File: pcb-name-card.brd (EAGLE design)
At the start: 87.5 x 54 mm, 7 parts

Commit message: aa banner
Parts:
- moved SW2 27.6 mm to (35.6, 5.70)
- moved SW1 27.4 mm to (35.7, 48.9)
- moved R1 14.2 mm to (64.3, 43.2), turned to 220 degrees
- moved R2 12.9 mm to (63.4, 10.7), turned to 145 degrees
- moved LED2 2.97 mm to (81.8, 23.1)
- moved U$1 1.21 mm to (12.1, 28.5)
- moved LED1 0.80 mm to (82.1, 31.8)
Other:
- board text added: "E:/Dropbox/git-projects/pcb-name-card/algoaccess banner.bmp"

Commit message: more changes
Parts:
- moved R1 8.28 mm to (58.6, 49.2), turned to 25 degrees
- moved R2 7.61 mm to (59.6, 4.11), turned to 335 degrees
- moved LED1 3.71 mm to (84.7, 34.4), turned to 0 degrees
- moved LED2 3.37 mm to (85.1, 22.4), turned to 0 degrees
- moved U$1 1.69 mm to (10.7, 27.6)
- moved SW1 1.27 mm to (35.7, 47.6)
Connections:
- net N$3: now also SW1.COM1; no longer SW1.COM2, U$1.+$2
- net N$4: now also SW1.CH2A; no longer SW1.CH1A
- net N$7: now also U$1.+$2; no longer SW1.COM1
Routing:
- net N$7: track 0.00 -> 28.2 mm
- net N$2: track 0.00 -> 27.0 mm
- net N$3: track 0.00 -> 26.9 mm
- net N$1: track 0.00 -> 25.3 mm
- net N$5: track 0.00 -> 18.0 mm
- net N$4: track 0.00 -> 17.0 mm
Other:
- board size 87.5 x 54 mm -> 87.5 x 53.3 mm
- board text added: "E:/Dropbox/git-projects/pcb-name-card/algoaccess banner mirror.bmp"

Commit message: some changes
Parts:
- moved R2 1.16 mm to (58.5, 4.39), turned to 330 degrees
- moved U$1 1.04 mm to (10.6, 26.5)
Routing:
- net N$6: track 0.00 -> 169.7 mm
- net N$7: track 28.2 -> 27.2 mm
- net N$5: track 18.0 -> 17.0 mm
- net N$2: track 27.0 -> 27.8 mm
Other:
- board text added: "Caution: Look away from LEDs before toggling the switches"
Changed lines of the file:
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@@
 <layer number="26" name="bNames" color="7" fill="1" visible="yes" active="yes"/>
 <layer number="27" name="tValues" color="7" fill="1" visible="no" active="yes"/>
-<layer number="28" name="bValues" color="7" fill="1" visible="no" active="yes"/>
+<layer number="28" name="bValues" color="7" fill="1" visible="yes" active="yes"/>
 <layer number="29" name="tStop" color="7" fill="3" visible="no" active="yes"/>
 <layer number="30" name="bStop" color="7" fill="6" visible="no" active="yes"/>
@@
 <layer number="43" name="vRestrict" color="2" fill="10" visible="no" active="yes"/>
 <layer number="44" name="Drills" color="7" fill="1" visible="no" active="yes"/>
-<layer number="45" name="Holes" color="7" fill="1" visible="yes" active="yes"/>
-<layer number="46" name="Milling" color="3" fill="1" visible="yes" active="yes"/>
+<layer number="45" name="Holes" color="7" fill="1" visible="no" active="yes"/>
+<layer number="46" name="Milling" color="3" fill="1" visible="no" active="yes"/>
 <layer number="47" name="Measures" color="7" fill="1" visible="no" active="yes"/>
 <layer number="48" name="Document" color="7" fill="1" visible="no" active="yes"/>
@@
 <layer number="120" name="KAP_MAAT1" color="7" fill="1" visible="no" active="no"/>
 <layer number="121" name="_tsilk" color="7" fill="1" visible="no" active="yes"/>
-<layer number="122" name="_bsilk" color="7" fill="1" visible="no" active="yes"/>
+<layer number="122" name="_bsilk" color="7" fill="1" visible="yes" active="yes"/>
 <layer number="123" name="tTestmark" color="7" fill="1" visible="no" active="yes"/>
 <layer number="124" name="bTestmark" color="7" fill="1" visible="no" active="yes"/>
@@
 <rectangle x1="53.29428125" y1="46.0400375" x2="53.721" y2="46.0705125" layer="22"/>
 <text x="0" y="-0.1524" size="0.060959375" layer="22" font="vector" rot="MR0">E:/Dropbox/git-projects/pcb-name-card/algoaccess banner mirror.bmp</text>
+<text x="30.9372" y="4.693921875" size="1.27" layer="22" font="vector" rot="MR0">Caution: Look away from LEDs
+before toggling the switches</text>
 </plain>
 <attributes>
@@
 <element name="LED1" library="led" package="PLCC2" value="UV" x="84.65185" y="34.44875" smashed="yes" rot="MR0">
 <attribute name="COLOR" value="yellow" x="84.65185" y="34.44875" size="1.778" layer="28" rot="MR0" display="off"/>
-<attribute name="VALUE" x="80.84185" y="32.54375" size="1.27" layer="28" rot="MR90"/>
+<attribute name="VALUE" x="80.84185" y="33.214309375" size="1.27" layer="28" rot="MR90"/>
 </element>
 <element name="LED2" library="led" package="CHIP-LED0805" value="Light" x="85.09635" y="22.39645" smashed="yes" rot="MR0">
-<attribute name="VALUE" x="81.9531" y="19.8247" size="1.27" layer="28" rot="MR90"/>
+<attribute name="VALUE" x="82.0140625" y="19.5808625" size="1.27" layer="28" rot="MR90"/>
 </element>
-<element name="U$1" library="cr2032" package="CR2032-SMD" value="" x="10.6807" y="27.570428125" smashed="yes" rot="MR270">
-<attribute name="VALUE" x="23.0307" y="31.888428125" size="1.6764" layer="28" font="vector" rot="MR270"/>
+<element name="U$1" library="cr2032" package="CR2032-SMD" value="" x="10.558778125" y="26.534109375" smashed="yes" rot="MR270">
+<attribute name="VALUE" x="22.908778125" y="30.852109375" size="1.6764" layer="28" font="vector" rot="MR270"/>
 </element>
 <element name="SW1" library="Seeed-OPL-Switch" package="SW6-2.54-SMD-7.0X3.5X1.5MM" value="" x="35.6743" y="47.63135" smashed="yes" rot="MR90">
@@
 </element>
 <element name="R1" library="resistor" package="0207/7" value="" x="58.6232" y="49.1998" smashed="yes" rot="MR25">
-<attribute name="NAME" x="59.17851875" y="48.488415625" size="1.27" layer="26" ratio="10" rot="MR25"/>
+<attribute name="NAME" x="59.239478125" y="48.244575" size="1.27" layer="26" ratio="10" rot="MR25"/>
 <attribute name="VALUE" x="60.458859375" y="47.72725" size="1.27" layer="28" ratio="10" rot="MR25"/>
 </element>
-<element name="R2" library="resistor" package="0207/7" value="" x="59.5884" y="4.1148" smashed="yes" rot="MR335">
-<attribute name="NAME" x="60.47875625" y="3.87030625" size="1.27" layer="26" ratio="10" rot="MR335"/>
-<attribute name="VALUE" x="61.89638125" y="4.5744625" size="1.27" layer="28" ratio="10" rot="MR335"/>
+<element name="R2" library="resistor" package="0207/7" value="" x="58.460640625" y="4.38911875" smashed="yes" rot="MR330">
+<attribute name="NAME" x="59.368915625" y="4.223153125" size="1.27" layer="26" ratio="10" rot="MR330"/>
+<attribute name="VALUE" x="60.719775" y="5.048184375" size="1.27" layer="28" ratio="10" rot="MR330"/>
 </element>
 </elements>
@@
 <contactref element="R2" pad="1"/>
 <contactref element="LED2" pad="A"/>
-<wire x1="63.041434375" y1="5.724975" x2="85.09635" y2="21.34645" width="0.4064" layer="16"/>
+<wire x1="61.7602" y1="6.29411875" x2="85.09635" y2="21.34645" width="0.4064" layer="16"/>
 </signal>
 <signal name="N$6">
@@
 <contactref element="LED1" pad="C"/>
 <contactref element="LED2" pad="C"/>
-<wire x1="85.09635" y1="23.44645" x2="84.65185" y2="32.74875" width="0" layer="19" extent="16-16"/>
-<wire x1="10.6807" y1="27.570428125" x2="84.65185" y2="32.74875" width="0" layer="19" extent="16-16"/>
+<wire x1="84.65185" y1="32.74875" x2="51.816" y2="49.408078125" width="0.4064" layer="16"/>
+<wire x1="51.816" y1="49.408078125" x2="10.558778125" y2="26.534109375" width="0.4064" layer="16"/>
+<wire x1="85.09635" y1="23.44645" x2="51.63311875" y2="3.84048125" width="0.4064" layer="16"/>
+<wire x1="51.63311875" y1="3.84048125" x2="10.558778125" y2="26.534109375" width="0.4064" layer="16"/>
 </signal>
 <signal name="N$3">
 <contactref element="U$1" pad="+$1"/>
 <contactref element="SW1" pad="COM1"/>
-<wire x1="10.6807" y1="39.000428125" x2="28.9179" y2="38.96995" width="0.4064" layer="16"/>
-<wire x1="28.9179" y1="38.96995" x2="35.6743" y2="44.45635" width="0.4064" layer="16"/>
+<wire x1="10.558778125" y1="37.964109375" x2="26.86558125" y2="37.964109375" width="0.4064" layer="16"/>
+<wire x1="26.86558125" y1="37.964109375" x2="35.6743" y2="44.45635" width="0.4064" layer="16"/>
 </signal>
 <signal name="N$7">
 <contactref element="U$1" pad="+$2"/>
 <contactref element="SW2" pad="COM2"/>
-<wire x1="10.6807" y1="16.140428125" x2="28.956" y2="16.1544" width="0.4064" layer="16"/>
-<wire x1="28.956" y1="16.1544" x2="35.6362" y2="8.87095" width="0.4064" layer="16"/>
+<wire x1="10.558778125" y1="15.104109375" x2="27.3913625" y2="15.104109375" width="0.4064" layer="16"/>
+<wire x1="27.3913625" y1="15.104109375" x2="35.6362" y2="8.87095" width="0.4064" layer="16"/>
 </signal>
 <signal name="N$5">
 <contactref element="R2" pad="2"/>
 <contactref element="SW2" pad="CH1A"/>
-<wire x1="56.13536875" y1="2.504621875" x2="38.1762" y2="2.52095" width="0.4064" layer="16"/>
+<wire x1="55.161084375" y1="2.484115625" x2="38.1762" y2="2.52095" width="0.4064" layer="16"/>
 </signal>
 <signal name="N$4">

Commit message: some updates
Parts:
- moved R2 12.1 mm to (69.5, 9.28)
- moved R1 10.7 mm to (68.4, 44.7)
- moved SW2 4.90 mm to (35.9, 10.6)
- moved SW1 4.55 mm to (36.3, 43.1)
- moved LED2 2.77 mm to (83.9, 19.9), turned to 180 degrees
- moved LED1 1.77 mm to (83.6, 33.0), turned to 180 degrees
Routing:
- net N$6: track 169.7 -> 220.7 mm
- net N$2: track 27.8 -> 14.8 mm
- net N$5: track 17.0 -> 27.7 mm
- net N$4: track 17.0 -> 26.1 mm
- net N$1: track 25.3 -> 16.7 mm
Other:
- board text added: "CR2025"

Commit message: more changes
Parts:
- moved SW1 2.54 mm to (36.3, 40.6)
- moved SW2 2.54 mm to (35.9, 13.1)
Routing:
- net N$7: track 27.0 -> 30.4 mm
- net N$3: track 27.4 -> 30.1 mm
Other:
- board text added: "Rev 1"
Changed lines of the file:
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@@
 <grid distance="0.1" unitdist="inch" unit="inch" style="lines" multiple="1" display="yes" altdistance="0.025" altunitdist="inch" altunit="inch"/>
 <layers>
-<layer number="1" name="Top" color="4" fill="1" visible="yes" active="yes"/>
+<layer number="1" name="Top" color="4" fill="1" visible="no" active="yes"/>
 <layer number="2" name="Route2" color="1" fill="3" visible="no" active="no"/>
 <layer number="3" name="Route3" color="4" fill="3" visible="no" active="no"/>
@@
 <layer number="19" name="Unrouted" color="6" fill="1" visible="yes" active="yes"/>
 <layer number="20" name="Dimension" color="15" fill="1" visible="yes" active="yes"/>
-<layer number="21" name="tPlace" color="7" fill="1" visible="yes" active="yes"/>
+<layer number="21" name="tPlace" color="7" fill="1" visible="no" active="yes"/>
 <layer number="22" name="bPlace" color="7" fill="1" visible="yes" active="yes"/>
-<layer number="23" name="tOrigins" color="15" fill="1" visible="yes" active="yes"/>
+<layer number="23" name="tOrigins" color="15" fill="1" visible="no" active="yes"/>
 <layer number="24" name="bOrigins" color="15" fill="1" visible="yes" active="yes"/>
-<layer number="25" name="tNames" color="7" fill="1" visible="yes" active="yes"/>
+<layer number="25" name="tNames" color="7" fill="1" visible="no" active="yes"/>
 <layer number="26" name="bNames" color="7" fill="1" visible="yes" active="yes"/>
-<layer number="27" name="tValues" color="7" fill="1" visible="yes" active="yes"/>
+<layer number="27" name="tValues" color="7" fill="1" visible="no" active="yes"/>
 <layer number="28" name="bValues" color="7" fill="1" visible="yes" active="yes"/>
 <layer number="29" name="tStop" color="7" fill="3" visible="no" active="yes"/>
@@
 <layer number="119" name="KAP_TEKEN" color="7" fill="1" visible="no" active="no"/>
 <layer number="120" name="KAP_MAAT1" color="7" fill="1" visible="no" active="no"/>
-<layer number="121" name="_tsilk" color="7" fill="1" visible="yes" active="yes"/>
+<layer number="121" name="_tsilk" color="7" fill="1" visible="no" active="yes"/>
 <layer number="122" name="_bsilk" color="7" fill="1" visible="yes" active="yes"/>
 <layer number="123" name="tTestmark" color="7" fill="1" visible="no" active="yes"/>
@@
 before toggling the switches</text>
 <text x="12.7" y="10.16" size="1.4224" layer="22" rot="MR0">CR2025</text>
+<text x="10.16" y="2.54" size="1.27" layer="22" rot="MR0">Rev 1</text>
 </plain>
 <attributes>
@@
 <attribute name="VALUE" x="22.908778125" y="30.852109375" size="1.6764" layer="28" font="vector" rot="MR270"/>
 </element>
-<element name="SW1" library="Seeed-OPL-Switch" package="SW6-2.54-SMD-7.0X3.5X1.5MM" value="" x="36.288984375" y="43.120309375" smashed="yes" rot="MR90">
-<attribute name="MPN" value="MS-22C01" x="36.288984375" y="43.120309375" size="1.778" layer="28" rot="MR90" display="off"/>
-<attribute name="NAME" x="36.695384375" y="44.441109375" size="0.889" layer="26" ratio="11" rot="MR270"/>
-<attribute name="VALUE" x="31.589984375" y="41.215309375" size="0.889" layer="28" ratio="11" rot="MR90"/>
+<element name="SW1" library="Seeed-OPL-Switch" package="SW6-2.54-SMD-7.0X3.5X1.5MM" value="" x="36.288984375" y="40.580309375" smashed="yes" rot="MR90">
+<attribute name="MPN" value="MS-22C01" x="36.288984375" y="40.580309375" size="1.778" layer="28" rot="MR90" display="off"/>
+<attribute name="NAME" x="36.695384375" y="41.901109375" size="0.889" layer="26" ratio="11" rot="MR270"/>
+<attribute name="VALUE" x="31.589984375" y="38.675309375" size="0.889" layer="28" ratio="11" rot="MR90"/>
 </element>
-<element name="SW2" library="Seeed-OPL-Switch" package="SW6-2.54-SMD-7.0X3.5X1.5MM" value="" x="35.941" y="10.5829125" smashed="yes" rot="MR90">
-<attribute name="MPN" value="MS-22C01" x="35.941" y="10.5829125" size="1.778" layer="28" rot="MR90" display="off"/>
-<attribute name="NAME" x="36.4998" y="11.8021125" size="0.889" layer="26" ratio="11" rot="MR270"/>
-<attribute name="VALUE" x="31.242" y="8.6779125" size="0.889" layer="28" ratio="11" rot="MR90"/>
+<element name="SW2" library="Seeed-OPL-Switch" package="SW6-2.54-SMD-7.0X3.5X1.5MM" value="" x="35.941" y="13.1229125" smashed="yes" rot="MR90">
+<attribute name="MPN" value="MS-22C01" x="35.941" y="13.1229125" size="1.778" layer="28" rot="MR90" display="off"/>
+<attribute name="NAME" x="36.4998" y="14.3421125" size="0.889" layer="26" ratio="11" rot="MR270"/>
+<attribute name="VALUE" x="31.242" y="11.2179125" size="0.889" layer="28" ratio="11" rot="MR90"/>
 </element>
 <element name="R1" library="resistor" package="0207/7" value="" x="68.3768" y="44.74971875" smashed="yes" rot="MR25">
@@
 <contactref element="U$1" pad="+$1"/>
 <contactref element="SW1" pad="COM1"/>
-<wire x1="10.558778125" y1="37.964109375" x2="22.86" y2="35.56" width="0.4064" layer="16"/>
-<wire x1="22.86" y1="35.56" x2="30.48" y2="35.56" width="0.4064" layer="16"/>
-<wire x1="30.48" y1="35.56" x2="36.288984375" y2="39.945309375" width="0.4064" layer="16"/>
+<wire x1="36.288984375" y1="37.405309375" x2="33.02" y2="33.02" width="0.4064" layer="16"/>
+<wire x1="33.02" y1="33.02" x2="15.24" y2="33.02" width="0.4064" layer="16"/>
+<wire x1="15.24" y1="33.02" x2="10.558778125" y2="37.964109375" width="0.4064" layer="16"/>
 </signal>
 <signal name="N$7">
 <contactref element="U$1" pad="+$2"/>
 <contactref element="SW2" pad="COM2"/>
-<wire x1="10.558778125" y1="15.104109375" x2="22.86" y2="17.78" width="0.4064" layer="16"/>
-<wire x1="22.86" y1="17.78" x2="30.48" y2="17.78" width="0.4064" layer="16"/>
-<wire x1="30.48" y1="17.78" x2="35.941" y2="13.7579125" width="0.4064" layer="16"/>
+<wire x1="35.941" y1="16.2979125" x2="33.02" y2="20.32" width="0.4064" layer="16"/>
+<wire x1="33.02" y1="20.32" x2="22.86" y2="20.32" width="0" layer="19" extent="1-16"/>
+<wire x1="10.558778125" y1="15.104109375" x2="10.16" y2="15.24" width="0.4064" layer="16"/>
+<wire x1="10.16" y1="15.24" x2="15.24" y2="20.32" width="0.4064" layer="16"/>
+<wire x1="15.24" y1="20.32" x2="33.02" y2="20.32" width="0.4064" layer="16"/>
 </signal>
 <signal name="N$5">
 <contactref element="R2" pad="2"/>
 <contactref element="SW2" pad="CH1A"/>
-<wire x1="66.179603125" y1="7.371075" x2="38.481" y2="7.4079125" width="0.4064" layer="16"/>
+<wire x1="38.481" y1="9.9479125" x2="45.72" y2="7.62" width="0.4064" layer="16"/>
+<wire x1="45.72" y1="7.62" x2="66.179603125" y2="7.371075" width="0.4064" layer="16"/>
 </signal>
 <signal name="N$4">
 <contactref element="R1" pad="2"/>
 <contactref element="SW1" pad="CH2A"/>
-<wire x1="64.92376875" y1="46.35989375" x2="38.828984375" y2="46.295309375" width="0.4064" layer="16"/>
+<wire x1="38.828984375" y1="43.755309375" x2="45.72" y2="45.72" width="0.4064" layer="16"/>
+<wire x1="45.72" y1="45.72" x2="64.92376875" y2="46.35989375" width="0.4064" layer="16"/>
 </signal>
 </signals>

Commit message: dimension
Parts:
- moved R2 0.72 mm to (69.9, 8.68)
- moved R1 0.67 mm to (68.7, 44.1)
- moved LED1 0.28 mm to (83.8, 32.8)
- moved SW1 0.28 mm to (36.5, 40.4)
- moved U$1 0.28 mm to (10.8, 26.3)
- moved SW2 0.28 mm to (36.1, 12.9)
- moved LED2 0.28 mm to (84.1, 19.7)
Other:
- board size 87.5 x 53.3 mm -> 87 x 53 mm

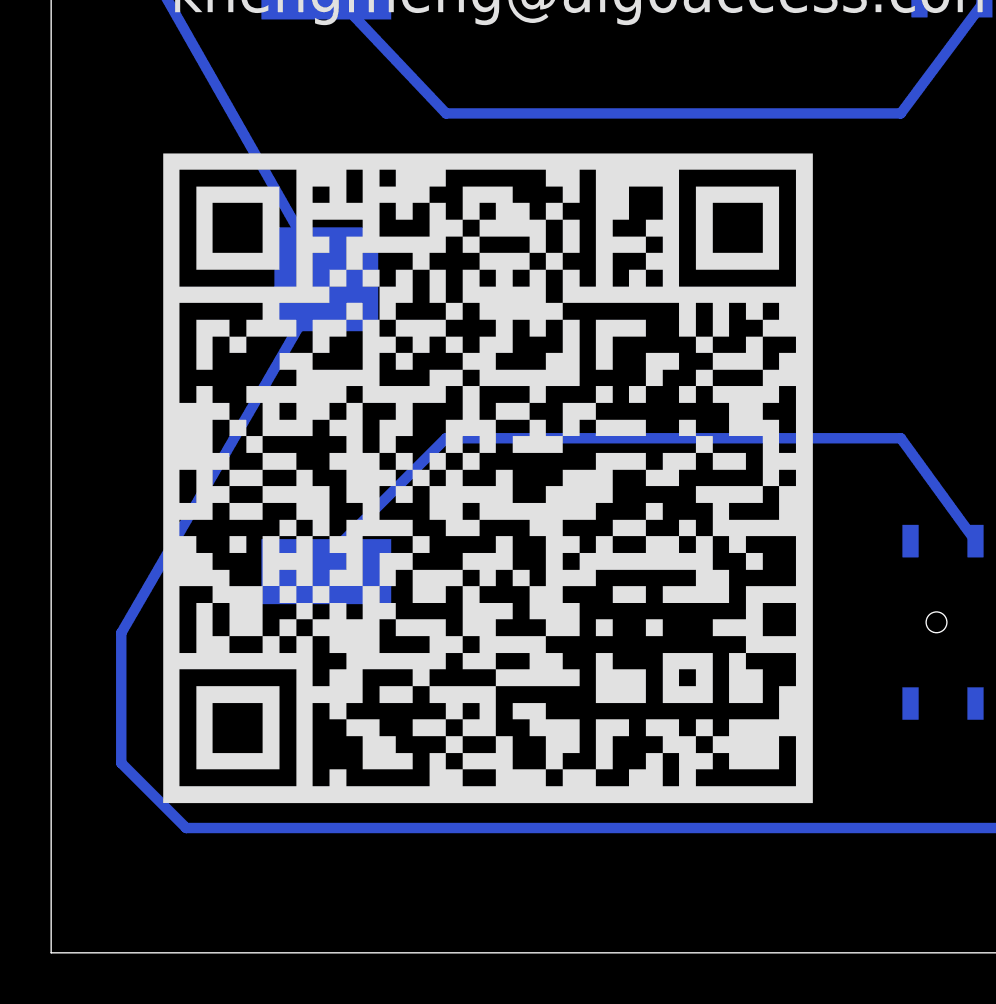
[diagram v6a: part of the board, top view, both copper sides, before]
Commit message: reimport qr code
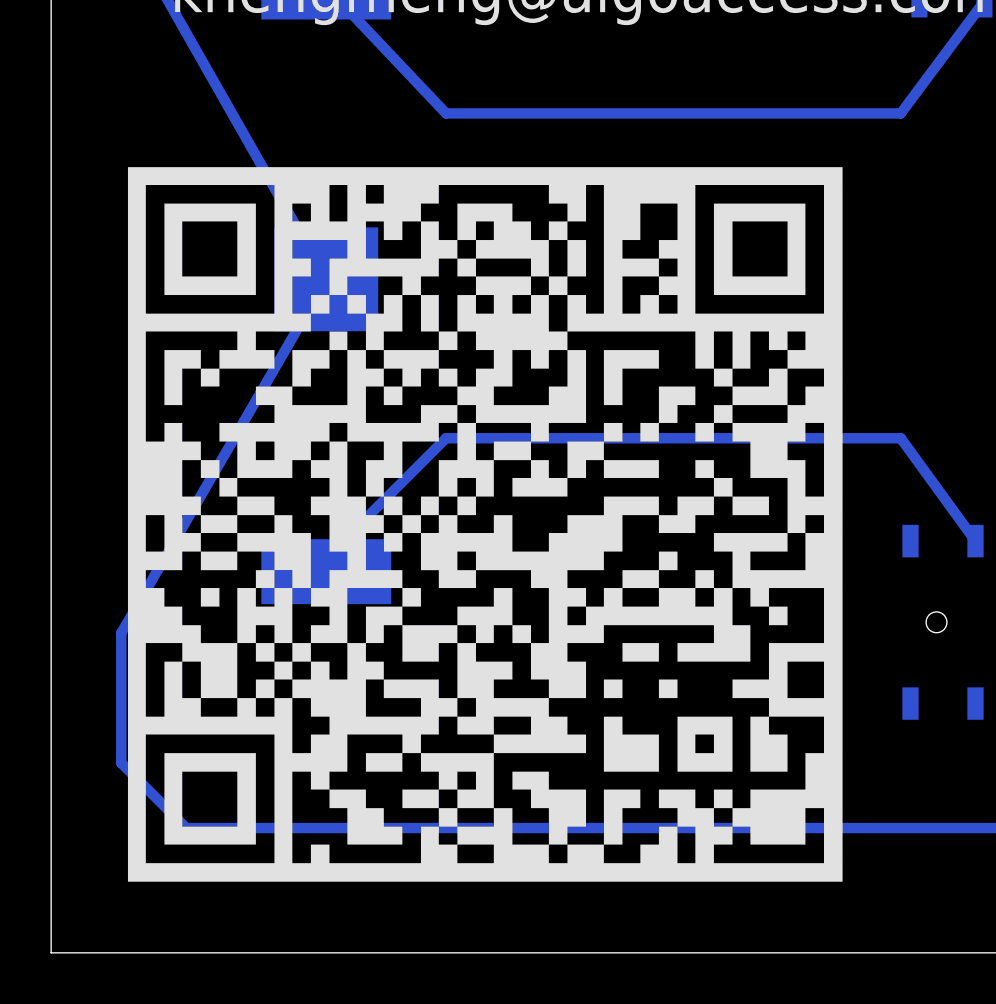
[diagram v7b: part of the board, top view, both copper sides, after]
